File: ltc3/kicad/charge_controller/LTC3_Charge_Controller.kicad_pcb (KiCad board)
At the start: 4 copper layers, 85.2 x 81.3 mm, 119 parts, among them P1 MicroFit header, P2 MicroFit header, P3 S2BPHKS, P4 MicroFit header, P5 JST XH header, P7 JST XH header, Q1 ZVN4525E6, Q2 BSC028N06NS, Q3 BSC028N06NS, Q4 BSC028N06NS, Q5 BSC028N06NS, Q6 ZVP3310F, Q7 MMBT5550L, U1 PI2127, U2 PI2127, U3 LT8490, U4 LTC2990

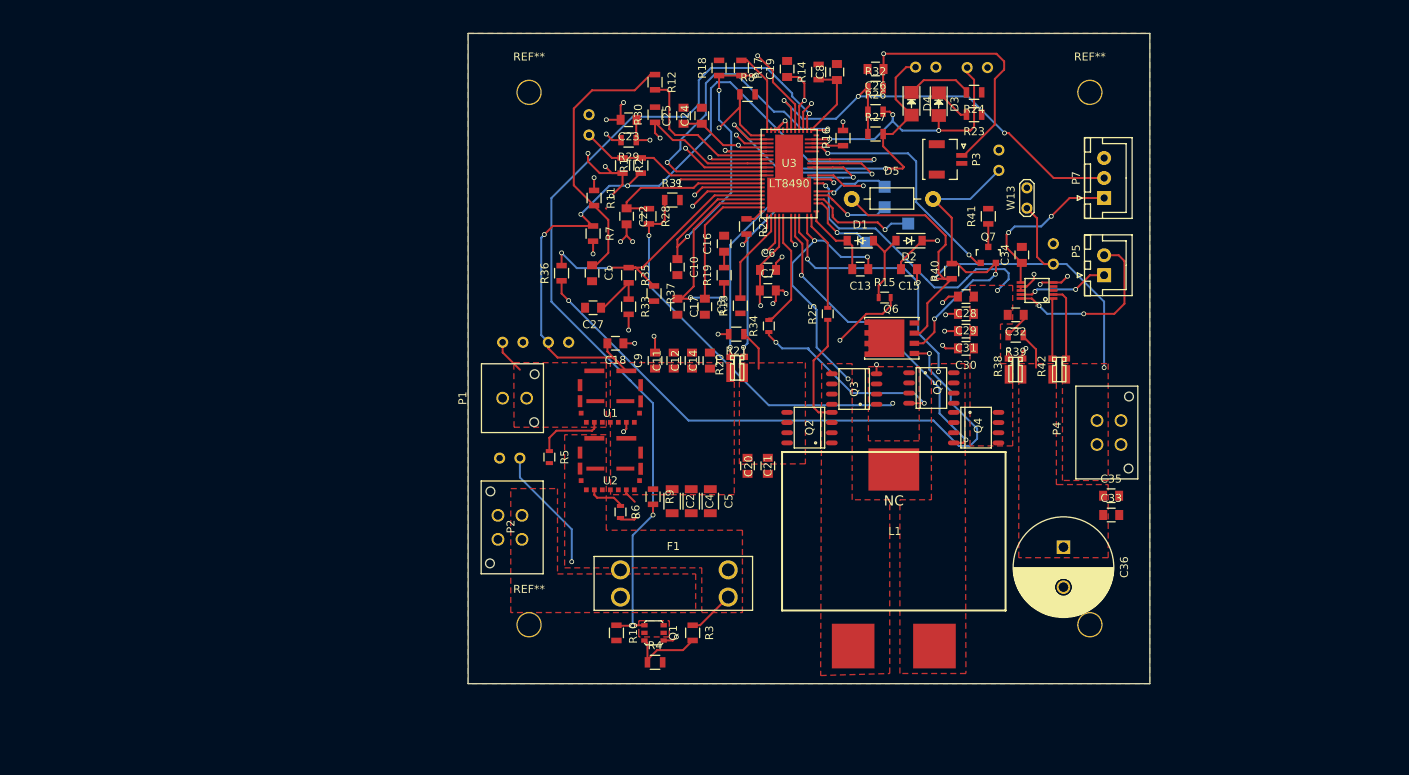
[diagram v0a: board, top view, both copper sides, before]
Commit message: LTC3: Layout
Moved silk screen references so they are visible.
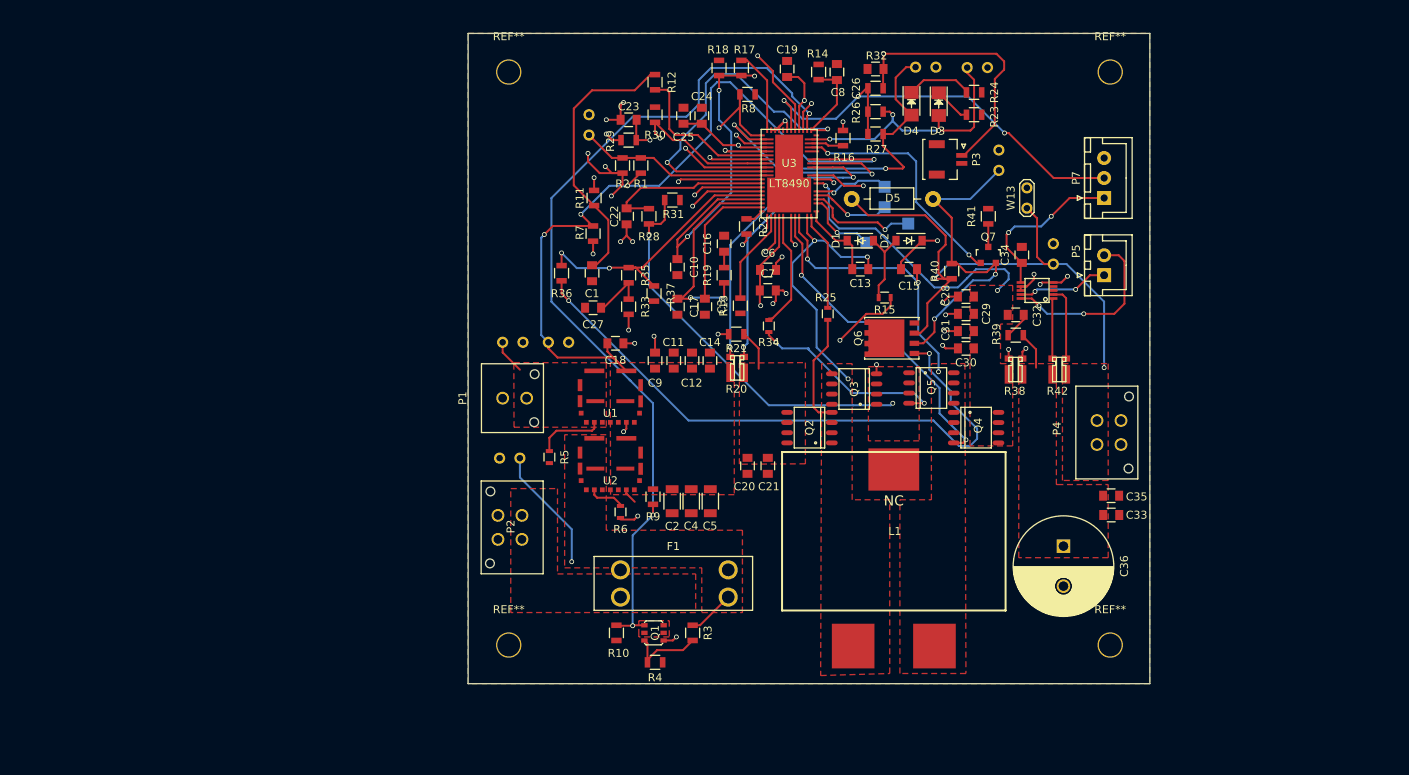
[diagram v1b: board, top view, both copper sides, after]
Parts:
- moved REF** 3.59 mm to (179.3, 67.1)
- moved REF** 3.59 mm to (104.1, 67.1)
- moved REF** 3.59 mm to (179.3, 138.7)
- moved REF** 3.59 mm to (104.1, 138.7)
- moved C36 0.13 mm to (173.5, 126.3)

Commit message: LTC3: Layout Review Notes
Had a layout review this morning (hooray!) and added "TODO" notes to all
the boards and schematics.  More work to be done!
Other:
- board text added: "Remove thermals for all power planes"
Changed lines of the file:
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@@
   (general
     (links 270)
-    (no_connects 0)
-    (area 96.304972 62.179999 187.159029 144.0641)
+    (no_connects 148)
+    (area 93.764972 61.6249 189.699029 144.2501)
     (thickness 1.6)
-    (drawings 4)
+    (drawings 5)
     (tracks 836)
     (zones 0)
@@
     (0 F.Cu signal)
     (1 Ground.Plane signal hide)
-    (2 In2.Cu signal)
-    (31 B.Cu signal)
-    (32 B.Adhes user)
-    (33 F.Adhes user)
+    (2 In2.Cu signal hide)
+    (31 B.Cu signal hide)
+    (32 B.Adhes user hide)
+    (33 F.Adhes user hide)
     (34 B.Paste user)
     (35 F.Paste user)
-    (36 B.SilkS user hide)
+    (36 B.SilkS user)
     (37 F.SilkS user)
     (38 B.Mask user)
@@
     (tags "capacitor 0805")
     (attr smd)
-    (fp_text reference C1 (at 2.54 0 360) (layer F.SilkS)
+    (fp_text reference C1 (at 2.54 0) (layer F.SilkS)
       (effects (font (size 1 1) (thickness 0.15)))
     )
@@
     (tags "capacitor 1206")
     (attr smd)
-    (fp_text reference C2 (at 3.1242 -0.0127 360) (layer F.SilkS)
+    (fp_text reference C2 (at 3.1242 -0.0127) (layer F.SilkS)
       (effects (font (size 1 1) (thickness 0.15)))
     )
@@
     (tags "capacitor 1206")
     (attr smd)
-    (fp_text reference C4 (at 3.0861 0.0254 360) (layer F.SilkS)
+    (fp_text reference C4 (at 3.0861 0.0254) (layer F.SilkS)
       (effects (font (size 1 1) (thickness 0.15)))
     )
@@
     (tags "capacitor 1206")
     (attr smd)
-    (fp_text reference C5 (at 3.0861 0.0381 360) (layer F.SilkS)
+    (fp_text reference C5 (at 3.0861 0.0381) (layer F.SilkS)
       (effects (font (size 1 1) (thickness 0.15)))
     )
@@
     (tags "capacitor 0805")
     (attr smd)
-    (fp_text reference C20 (at 2.5908 0.381 360) (layer F.SilkS)
+    (fp_text reference C20 (at 2.5908 0.381) (layer F.SilkS)
       (effects (font (size 1 1) (thickness 0.15)))
     )
@@
     (tags "capacitor 0805")
     (attr smd)
-    (fp_text reference C21 (at 2.5908 -0.127 360) (layer F.SilkS)
+    (fp_text reference C21 (at 2.5908 -0.127) (layer F.SilkS)
       (effects (font (size 1 1) (thickness 0.15)))
     )
@@
     (tags "resistor 0805")
     (attr smd)
-    (fp_text reference R2 (at 2.286 0 360) (layer F.SilkS)
+    (fp_text reference R2 (at 2.286 0) (layer F.SilkS)
       (effects (font (size 1 1) (thickness 0.15)))
     )
@@
     (tags "resistor 0805")
     (attr smd)
-    (fp_text reference R3 (at 0 -1.905 450) (layer F.SilkS)
+    (fp_text reference R3 (at 0 -1.905 90) (layer F.SilkS)
       (effects (font (size 1 1) (thickness 0.15)))
     )
@@
     (tags "resistor 0805")
     (attr smd)
-    (fp_text reference R9 (at 2.4892 0 360) (layer F.SilkS)
+    (fp_text reference R9 (at 2.4892 0) (layer F.SilkS)
       (effects (font (size 1 1) (thickness 0.15)))
     )
@@
     (tags "resistor 0805")
     (attr smd)
-    (fp_text reference R10 (at 2.54 -0.254 360) (layer F.SilkS)
+    (fp_text reference R10 (at 2.54 -0.254) (layer F.SilkS)
       (effects (font (size 1 1) (thickness 0.15)))
     )
@@
     (tags "resistor 0805")
     (attr smd)
-    (fp_text reference R17 (at -2.286 -0.381 360) (layer F.SilkS)
+    (fp_text reference R17 (at -2.286 -0.381) (layer F.SilkS)
       (effects (font (size 1 1) (thickness 0.15)))
     )
@@
     (tags "resistor 0805")
     (attr smd)
-    (fp_text reference R28 (at 2.54 0 360) (layer F.SilkS)
+    (fp_text reference R28 (at 2.54 0) (layer F.SilkS)
       (effects (font (size 1 1) (thickness 0.15)))
     )
@@
     (tags "LED1206 SMD")
     (attr smd)
-    (fp_text reference D3 (at 3.3528 0.1524 360) (layer F.SilkS)
+    (fp_text reference D3 (at 3.3528 0.1524) (layer F.SilkS)
       (effects (font (size 1 1) (thickness 0.15)))
     )
@@
     (tags "LED1206 SMD")
     (attr smd)
-    (fp_text reference D4 (at 3.4036 0.0508 360) (layer F.SilkS)
+    (fp_text reference D4 (at 3.4036 0.0508) (layer F.SilkS)
       (effects (font (size 1 1) (thickness 0.15)))
     )
@@
     (tags "resistor 0603")
     (attr smd)
-    (fp_text reference R6 (at 2.159 0 360) (layer F.SilkS)
+    (fp_text reference R6 (at 2.159 0) (layer F.SilkS)
       (effects (font (size 1 1) (thickness 0.15)))
     )
@@
     )
   )
+  (gr_text "Remove thermals for all power planes" (at 76.2 111.506) (layer F.Mask)
+    (effects (font (size 1.5 1.5) (thickness 0.3)))
+  )
   (gr_line (start 184.277 143.51) (end 99.06 143.51) (angle 90) (layer Edge.Cuts) (width 0.1))
   (gr_line (start 184.277 62.23) (end 184.277 143.51) (angle 90) (layer Edge.Cuts) (width 0.1))
@@
     (connect_pads yes (clearance 0.381))
     (min_thickness 0.254)
-    (fill yes (arc_segments 16) (thermal_gap 0.508) (thermal_bridge_width 0.508))
+    (fill (arc_segments 16) (thermal_gap 0.508) (thermal_bridge_width 0.508))
     (polygon
       (pts
@@
     (connect_pads (clearance 0.508))
     (min_thickness 0.254)
-    (fill yes (arc_segments 16) (thermal_gap 0.508) (thermal_bridge_width 0.508))
+    (fill (arc_segments 16) (thermal_gap 0.508) (thermal_bridge_width 0.508))
     (polygon
       (pts
@@
     (connect_pads (clearance 0.381))
     (min_thickness 0.254)
-    (fill yes (arc_segments 16) (thermal_gap 0.508) (thermal_bridge_width 0.508))
+    (fill (arc_segments 16) (thermal_gap 0.508) (thermal_bridge_width 0.508))
     (polygon
       (pts
@@
     (connect_pads (clearance 0.508))
     (min_thickness 0.254)
-    (fill yes (arc_segments 16) (thermal_gap 0.508) (thermal_bridge_width 0.508))
+    (fill (arc_segments 16) (thermal_gap 0.508) (thermal_bridge_width 0.508))
     (polygon
       (pts
@@
     (connect_pads (clearance 0.508))
     (min_thickness 0.254)
-    (fill yes (arc_segments 16) (thermal_gap 0.508) (thermal_bridge_width 0.508))
+    (fill (arc_segments 16) (thermal_gap 0.508) (thermal_bridge_width 0.508))
     (polygon
       (pts
@@
     (connect_pads (clearance 0.508))
     (min_thickness 0.254)
-    (fill yes (arc_segments 16) (thermal_gap 0.508) (thermal_bridge_width 0.508))
+    (fill (arc_segments 16) (thermal_gap 0.508) (thermal_bridge_width 0.508))
     (polygon
       (pts
@@
     (connect_pads (clearance 0.508))
     (min_thickness 0.254)
-    (fill yes (arc_segments 16) (thermal_gap 0.508) (thermal_bridge_width 0.508))
+    (fill (arc_segments 16) (thermal_gap 0.508) (thermal_bridge_width 0.508))
     (polygon
       (pts
@@
     (connect_pads (clearance 0.508))
     (min_thickness 0.254)
-    (fill yes (arc_segments 16) (thermal_gap 0.508) (thermal_bridge_width 0.508))
+    (fill (arc_segments 16) (thermal_gap 0.508) (thermal_bridge_width 0.508))
     (polygon
       (pts
@@
     (connect_pads (clearance 0.508))
     (min_thickness 0.254)
-    (fill yes (arc_segments 16) (thermal_gap 0.508) (thermal_bridge_width 0.508))
+    (fill (arc_segments 16) (thermal_gap 0.508) (thermal_bridge_width 0.508))
     (polygon
       (pts
@@
     (connect_pads yes (clearance 0.508))
     (min_thickness 0.254)
-    (fill yes (arc_segments 16) (thermal_gap 0.508) (thermal_bridge_width 0.508))
+    (fill (arc_segments 16) (thermal_gap 0.508) (thermal_bridge_width 0.508))
     (polygon
       (pts
@@
     (connect_pads (clearance 0.508))
     (min_thickness 0.254)
-    (fill yes (arc_segments 16) (thermal_gap 0.508) (thermal_bridge_width 0.508))
+    (fill (arc_segments 16) (thermal_gap 0.508) (thermal_bridge_width 0.508))
     (polygon
       (pts
@@
     (connect_pads (clearance 0.508))
     (min_thickness 0.254)
-    (fill yes (arc_segments 16) (thermal_gap 0.508) (thermal_bridge_width 0.508))
+    (fill (arc_segments 16) (thermal_gap 0.508) (thermal_bridge_width 0.508))
     (polygon
       (pts
@@
     (connect_pads (clearance 0.508))
     (min_thickness 0.254)
-    (fill yes (arc_segments 16) (thermal_gap 0.508) (thermal_bridge_width 0.508))
+    (fill (arc_segments 16) (thermal_gap 0.508) (thermal_bridge_width 0.508))
     (polygon
       (pts
@@
     (connect_pads (clearance 0.508))
     (min_thickness 0.254)
-    (fill yes (arc_segments 16) (thermal_gap 0.508) (thermal_bridge_width 0.508))
+    (fill (arc_segments 16) (thermal_gap 0.508) (thermal_bridge_width 0.508))
     (polygon
       (pts
